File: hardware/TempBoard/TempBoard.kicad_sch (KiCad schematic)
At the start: 1 part, among them J1 MX150_02x10_Vertical

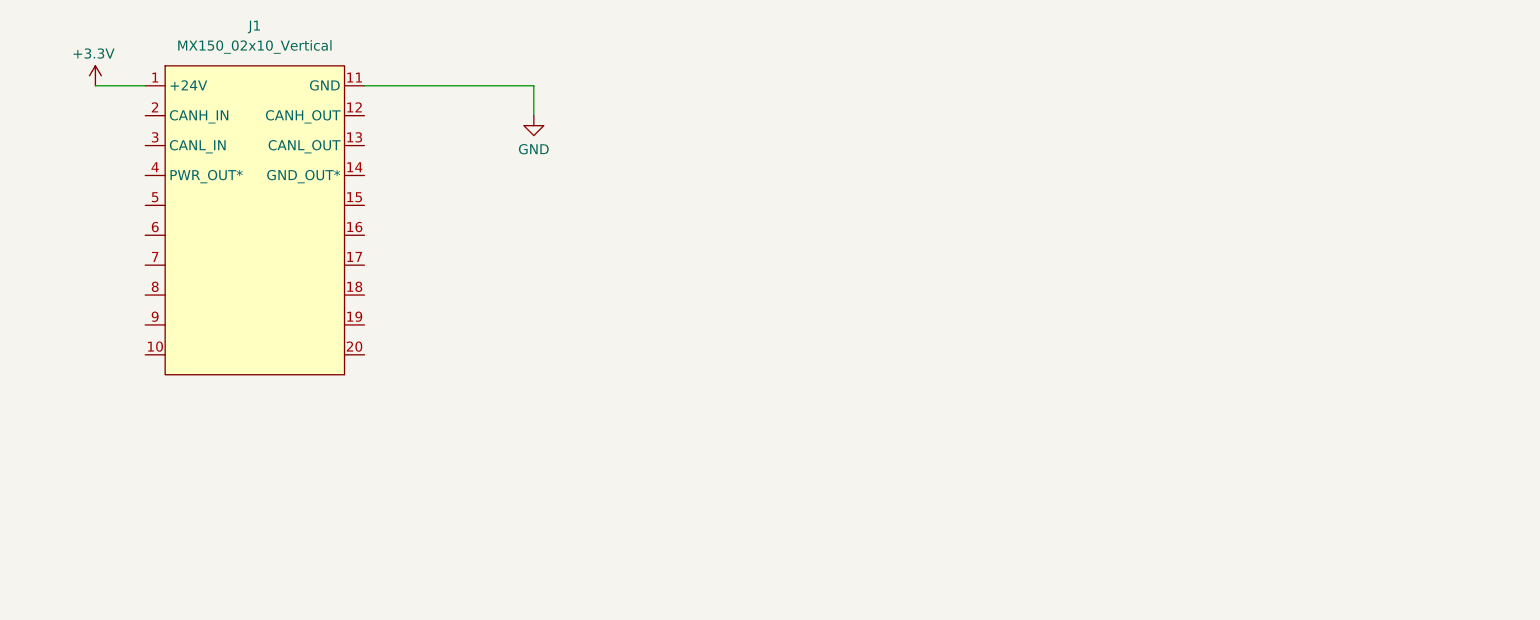
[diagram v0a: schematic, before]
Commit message: Temperature board schematic partially complete without testpoints.
Signed-off-by: Karthik Kurapati <kkurapati10@gmail.com>
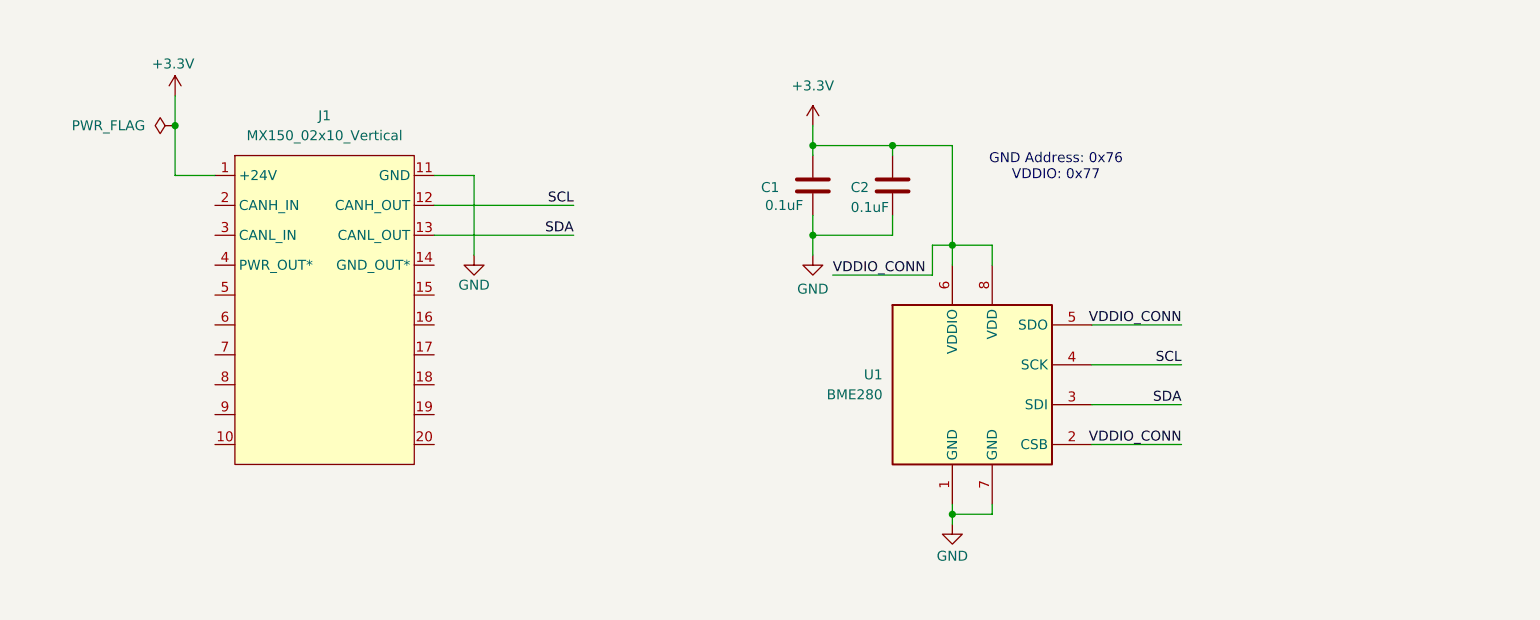
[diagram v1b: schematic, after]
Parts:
- added C1, C2: 0.1uF, symbol Device:C
- added U1: BME280, Package_LGA:Bosch_LGA-8_2.5x2.5mm_P0.65mm_ClockwisePinNumbering, symbol Sensor:BME280
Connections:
- net +3.3V: now also C1.1, C2.1, U1.2 (CSB), U1.5 (SDO), U1.6 (VDDIO), U1.8 (VDD)
- net GND: now also C1.2, C2.2, U1.1 (GND), U1.7 (GND)
- net SCL: now reaches J1.12 (CANH_OUT)
- net SCL: now also U1.4 (SCK)
- net SDA: now reaches J1.13 (CANL_OUT)
- net SDA: now also U1.3 (SDI)
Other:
- note added: "GND Address: 0x76 VDDIO: 0x77"
- moved on the sheet: J1

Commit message: finished schematic for all
Signed-off-by: Vortex-Overdrive <kkurapati10@gmail.com>
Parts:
- removed J1: MX150_02x10_Vertical, UTSVT_Connectors:CONN_SD-75757-002_2X10_F16p09_MOL, symbol utsvt_connectors:MX150_02x10_Vertical
- added 3.3vTP1, GNDTP1, GNDTP2, GNDTP3, SCL_TP1, SCL_TP2: TestPoint, symbol Connector:TestPoint
- added C3: 10uF, symbol Device:C
- added D1: LED, symbol Device:LED
- added J2: Conn_01x05, symbol Connector_Generic:Conn_01x05
- added R1, R2, R3: 100, symbol Device:R
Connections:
- net +3.3V: now also 3.3vTP1.1, C3.1, J2.5 (Pin_5), R1.1, R2.1, R3.1
- net GND: now also C3.2, D1.1 (K), GNDTP1.1, GNDTP2.1, GNDTP3.1, J2.2 (Pin_2)
- net SCL: now also J2.4 (Pin_4), R2.2, SCL_TP1.1
- net SDA: now also J2.3 (Pin_3), R3.2, SCL_TP2.1
- new net: D1.2 (A), R1.2
- no-connect marks 0 -> 1
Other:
- moved on the sheet: C1, C2, U1

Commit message: small changes
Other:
- note added: "Connectors will probably be nanofit"
- note added: "I2C is enabled when CSB is connected to VDDIO"
- note added: "SDO --> address bit"
- title: (none) -> Temperature / Humidity Board
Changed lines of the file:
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@@
 	(generator_version "9.0")
 	(paper "A4")
+	(title_block
+		(title "Temperature / Humidity Board")
+		(date "2025-10-27")
+		(rev "A")
+	)
+	(text "Connectors will \nprobably be nanofit"
+		(exclude_from_sim no)
+		(at 185.674 23.114 0)
+		(effects
+			(font
+				(size 1.27 1.27)
+			)
+		)
+	)
+	(text "I2C is enabled when CSB\nis connected to VDDIO"
+		(exclude_from_sim no)
+		(at 94.996 68.834 0)
+		(effects
+			(font
+				(size 1.27 1.27)
+			)
+		)
+	)
 	(text "GND Address: 0x76\nVDDIO: 0x77\n"
 		(exclude_from_sim no)
@@
 		(effects
 			(font
+				(size 1.27 1.27)
+			)
+		)
+	)
+	(text "SDO --> address bit"
+		(exclude_from_sim no)
+		(at 94.234 73.914 0)
+		(effects
+			(font

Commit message: added op-amp, finished footprints, new connector, fuse, ldo
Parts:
- added R4: 0, symbol Device:R
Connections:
- net +3.3V: now also R4.2; no longer U1.5 (SDO)
- new net: R4.1, U1.5 (SDO)
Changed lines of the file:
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@@
 	(wire
 		(pts
-			(xy 68.58 52.07) (xy 80.01 52.07)
+			(xy 68.58 52.07) (xy 69.85 52.07)
 		)
 		(stroke
@@
 	(wire
 		(pts
+			(xy 83.82 41.91) (xy 80.01 41.91)
+		)
+		(stroke
+			(width 0)
+			(type default)
+		)
+	)
+	(wire
+		(pts
 			(xy 157.48 34.29) (xy 157.48 38.1)
 		)
@@
 	(wire
 		(pts
+			(xy 83.82 41.91) (xy 83.82 52.07)
+		)
+		(stroke
+			(width 0)
+			(type default)
+		)
+	)
+	(wire
+		(pts
 			(xy 22.86 38.1) (xy 22.86 40.64)
 		)
@@
 		(pts
 			(xy 48.26 41.91) (xy 48.26 48.26)
+		)
+		(stroke
+			(width 0)
+			(type default)
+		)
+	)
+	(wire
+		(pts
+			(xy 83.82 52.07) (xy 77.47 52.07)
 		)
 		(stroke
@@
 	)
 	(label "VDDIO_CONN"
-		(at 80.01 52.07 180)
+		(at 80.01 41.91 180)
 		(effects
 			(font
@@
 					(unit 1)
 				)
+			)
+		)
+	)
+	(symbol
+		(lib_id "Device:R")
+		(at 73.66 52.07 90)
+		(unit 1)
+		(exclude_from_sim no)
+		(in_bom yes)
+		(on_board yes)
+		(dnp no)
+		(property "Reference" "R4"
+			(at 73.406 49.53 90)
+			(effects
+				(font
+					(size 1.27 1.27)
+				)
+			)
+		)
+		(property "Value" "0"
+			(at 73.66 54.356 90)
+			(effects
+				(font
+					(size 1.27 1.27)
+				)
+			)
+		)
+		(property "Footprint" ""
+			(at 73.66 53.848 90)
+			(effects
+				(font
+					(size 1.27 1.27)
+				)
+				(hide yes)
+			)
+		)
+		(property "Datasheet" "~"
+			(at 73.66 52.07 0)
+			(effects
+				(font
+					(size 1.27 1.27)
+				)
+				(hide yes)
+			)
+		)
+		(property "Description" "Resistor"
+			(at 73.66 52.07 0)
+			(effects
+				(font
+					(size 1.27 1.27)
+				)
+				(hide yes)
+			)
+		)
+		(pin "1"
+		)
+		(pin "2"
+		)
+		(instances
+			(project ""
+				(path "/9258ccab-0ef6-442d-b425-b92e09dff747"
+					(reference "R4")
+					(unit 1)
+				)

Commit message: finished rev a layout for all 3 boards + added cubemx file
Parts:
- removed GNDTP1, GNDTP2, GNDTP3, SCL_TP1, SCL_TP2: TestPoint, symbol Connector:TestPoint
- removed J2: Conn_01x05, symbol Connector_Generic:Conn_01x05
- added GND_TP1: TestPoint, TestPoint:TestPoint_Pad_1.0x1.0mm, symbol Connector:TestPoint
- added H1, H2, H3, H4: MountingHole, MountingHole:MountingHole_2.2mm_M2, symbol Mechanical:MountingHole
- added J1: Conn_01x04, Connector_Molex:Molex_Nano-Fit_105309-xx04_1x04_P2.50mm_Vertical, symbol Connector_Generic:Conn_01x04
- added J2: Conn_01x03, Connector_PinHeader_2.54mm:PinHeader_1x03_P2.54mm_Vertical, symbol Connector_Generic:Conn_01x03
- 3.3vTP1: footprint (none) -> TestPoint:TestPoint_Pad_1.0x1.0mm
- C1, C2: footprint (none) -> Capacitor_SMD:C_0603_1608Metric_Pad1.08x0.95mm_HandSolder; P/N (none) -> MLASH168SB7104KTNA01
- C3: footprint (none) -> Capacitor_SMD:C_0603_1608Metric_Pad1.08x0.95mm_HandSolder; P/N (none) -> GRM21BR61H106KE43K
- D1: footprint (none) -> LED_SMD:LED_0603_1608Metric_Pad1.05x0.95mm_HandSolder; P/N (none) -> NCD0603R1
- R1: value 100 -> 1k; footprint (none) -> Resistor_SMD:R_0603_1608Metric_Pad0.98x0.95mm_HandSolder; P/N (none) -> CRCW06031K00FKEI
- R2, R3: value 100 -> 4.6k; footprint (none) -> Resistor_SMD:R_0603_1608Metric_Pad0.98x0.95mm_HandSolder; P/N (none) -> CRCW06034K70FKEA
- R4: footprint (none) -> Resistor_SMD:R_0603_1608Metric_Pad0.98x0.95mm_HandSolder; P/N (none) -> CRCW06030000Z0EE
- U1: P/N (none) -> 828-1063-6-ND
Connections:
- net +3.3V: now also J1.4 (Pin_4)
- net GND: now also GND_TP1.1, J1.1 (Pin_1), J2.3 (Pin_3)
- net SCL: now also J1.3 (Pin_3), J2.1 (Pin_1)
- net SDA: now also J1.2 (Pin_2), J2.2 (Pin_2)
- no-connect marks 1 -> 0

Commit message: finished irboard, tempboard
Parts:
- H1, H2, H3, H4: footprint MountingHole:MountingHole_2.2mm_M2 -> MountingHole:MountingHole_3.2mm_M3
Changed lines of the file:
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@@
 			)
 		)
-		(property "Footprint" "MountingHole:MountingHole_2.2mm_M2"
+		(property "Footprint" "MountingHole:MountingHole_3.2mm_M3"
 			(at 189.23 54.61 0)
 			(effects
@@
 			)
 		)
-		(property "Footprint" "MountingHole:MountingHole_2.2mm_M2"
+		(property "Footprint" "MountingHole:MountingHole_3.2mm_M3"
 			(at 189.23 60.96 0)
 			(effects
@@
 			)
 		)
-		(property "Footprint" "MountingHole:MountingHole_2.2mm_M2"
+		(property "Footprint" "MountingHole:MountingHole_3.2mm_M3"
 			(at 189.23 67.31 0)
 			(effects
@@
 			)
 		)
-		(property "Footprint" "MountingHole:MountingHole_2.2mm_M2"
+		(property "Footprint" "MountingHole:MountingHole_3.2mm_M3"
 			(at 189.23 48.26 0)
 			(effects

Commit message: finished ir_board, temp_board with horizontal connectors
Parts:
- J1: footprint Connector_Molex:Molex_Nano-Fit_105309-xx04_1x04_P2.50mm_Vertical -> Connector_Molex:Molex_Nano-Fit_105313-xx04_1x04_P2.50mm_Horizontal
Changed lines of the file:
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@@
 			)
 		)
-		(property "Footprint" "Connector_Molex:Molex_Nano-Fit_105309-xx04_1x04_P2.50mm_Vertical"
+		(property "Footprint" "Connector_Molex:Molex_Nano-Fit_105313-xx04_1x04_P2.50mm_Horizontal"
 			(at 132.08 31.75 0)
 			(effects

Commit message: .bom files generated, cleaned up pitot board.
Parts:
- J1: P/N 538-105309-1304 -> 105313-1104
- U1: P/N 828-1063-6-ND -> BME280
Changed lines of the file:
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@@
 			)
 		)
-		(property "P/N" "828-1063-6-ND"
+		(property "P/N" "BME280"
 			(at 53.34 59.69 0)
 			(effects
@@
 			)
 		)
-		(property "P/N" "538-105309-1304"
+		(property "P/N" "105313-1104"
 			(at 132.08 31.75 0)
 			(effects
